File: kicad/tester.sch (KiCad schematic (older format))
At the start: 44 parts

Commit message: Schematic capture almost complete
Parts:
- added DS?: LCD16X2, WC1602A, symbol LCD16X2
- added R?: 270, symbol R_Small
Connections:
- net GND: now also DS?.16 (LED-)
- net VCC: now also R?.1
- net at IC?.11 ((PCINT21/OC0B/T1)PD5): now also DS?.6 (E)
- net at IC?.2 ((PCINT16/RXD)PD0): now also DS?.11 (D4)
- net at IC?.3 ((PCINT17/TXD)PD1): now also DS?.12 (D5)
- net at IC?.4 ((PCINT18/INT0)PD2): now also DS?.13 (D6)
- net at IC?.5 ((PCINT19/OC2B/INT1)PD3): now also DS?.14 (D7)
- net at IC?.6 ((PCINT20/XCK/T0)PD4): now also DS?.4 (RS)
- new net: DS?.15 (LED+), R?.2
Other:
- moved on the sheet: BT?, C?, CON?, D?, IC?, P?, Q?, R?, SW?, U?, Y?

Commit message: Schematic complete. Some refs des. incomplete
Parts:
- added R?: 10K, symbol R_Small
- added RV?: POT, symbol POT
- gave numbers to parts that had none: 19
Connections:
- net GND: now also C1.1, C3.1, DS?.1 (VSS), DS?.5 (R/W), RV?.3; no longer C1.2, C3.2
- net VCC: now also C3.2, DS?.2 (VDD), R?.1; no longer C3.1
- net at U1.21 (AREF): now also C1.2; no longer C1.1
- net at DS?.3 (VO): now also RV?.2
- new net: R?.2, RV?.1
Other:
- moved on the sheet: C1, C10, C3, C4, DS?

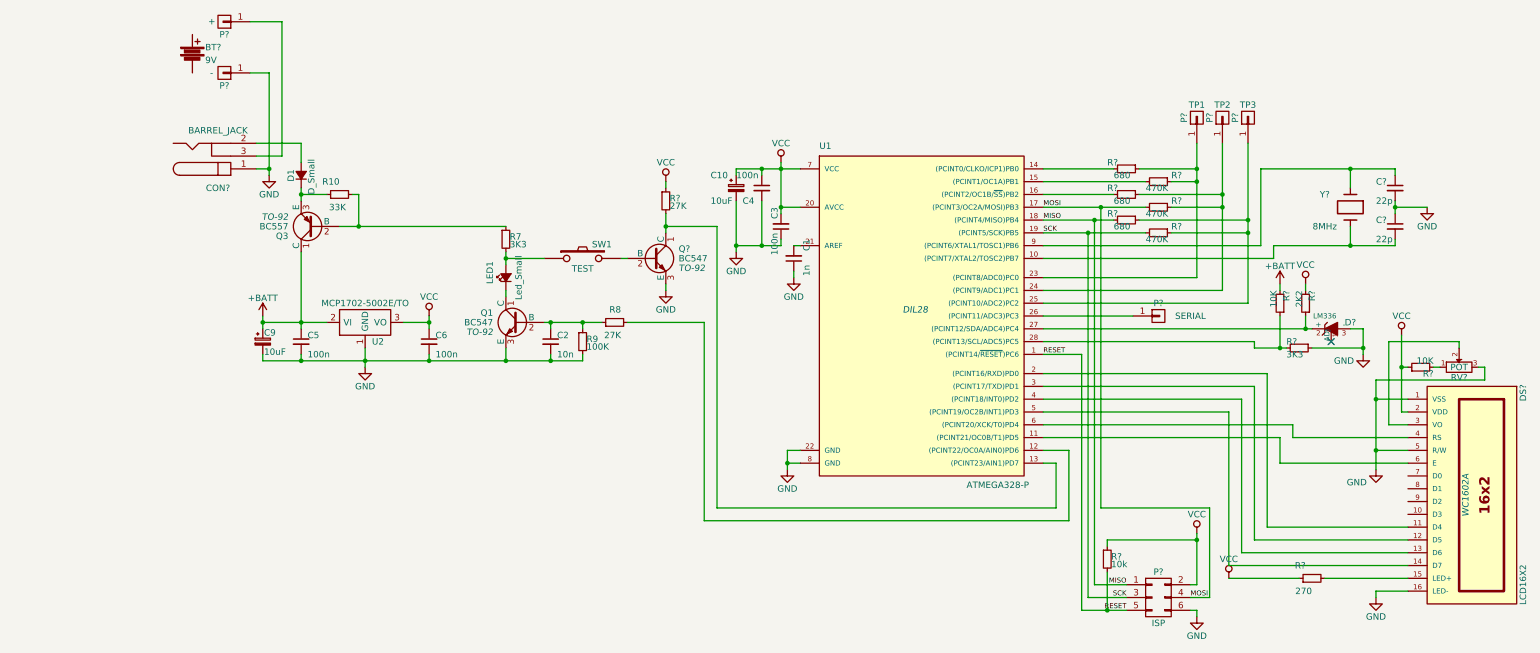
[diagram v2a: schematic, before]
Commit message: Board routing almost done
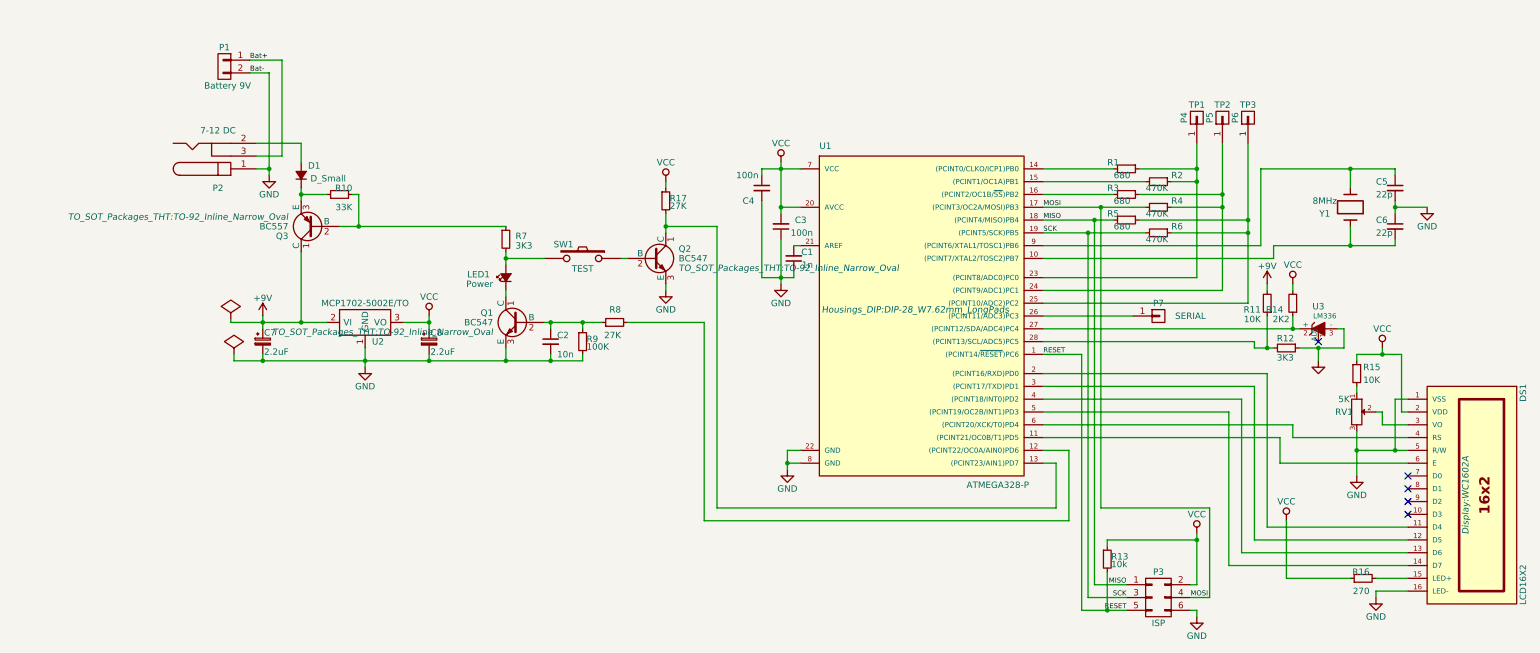
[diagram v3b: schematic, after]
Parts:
- removed BT?: 9V, symbol Battery
- removed C10: 10uF, symbol CP_Small
- removed C5, C6: 100n, symbol C_Small
- removed P?: +, symbol CONN_01X01
- removed P?: -, symbol CONN_01X01
- added C8: 2.2uF, Capacitors_ThroughHole:C_Radial_D6.3_L11.2_P2.5, symbol CP_Small
- added P1: Battery 9V, Connect:PINHEAD1-2, symbol CONN_01X02
- C1, C2: footprint (none) -> Capacitors_ThroughHole:C_Disc_D3_P2.5
- C3, C4: footprint (none) -> Capacitors_ThroughHole:C_Disc_D6_P5
- C5, C6: renamed from C?; footprint (none) -> Capacitors_ThroughHole:C_Disc_D3_P2.5
- C7: renamed from C9; value 10uF -> 2.2uF; footprint (none) -> Capacitors_ThroughHole:C_Radial_D6.3_L11.2_P2.5
- D1: footprint (none) -> Diodes_ThroughHole:Diode_DO-35_SOD27_Horizontal_RM10
- DS1: renamed from DS?; footprint WC1602A -> Display:WC1602A
- LED1: value Led_Small -> Power; footprint (none) -> LEDs:LED-3MM
- P2: renamed from CON?; value BARREL_JACK -> 7-12 DC; footprint (none) -> Connect:BARREL_JACK
- P3: renamed from P?; footprint (none) -> Pin_Headers:Pin_Header_Straight_2x03
- P4, P5, P6, P7: renamed from P?; footprint (none) -> Wire_Pads:SolderWirePad_single_1mmDrill
- Q1, Q3: footprint TO-92 -> TO_SOT_Packages_THT:TO-92_Inline_Narrow_Oval
- Q2: renamed from Q?; footprint TO-92 -> TO_SOT_Packages_THT:TO-92_Inline_Narrow_Oval
- R1, R11, R12, R13, R14, R15, R16, R17, R2, R3, R4, R5, R6: renamed from R?; footprint (none) -> Resistors_ThroughHole:Resistor_Horizontal_RM10mm
- R10, R7, R8, R9: footprint (none) -> Resistors_ThroughHole:Resistor_Horizontal_RM10mm
- RV1: renamed from RV?; value POT -> 5K; footprint (none) -> Potentiometers:Potentiometer_VishaySpectrol-Econtrim-Type36k
- SW1: footprint (none) -> Connect:PINHEAD1-2
- U1: footprint DIL28 -> Housings_DIP:DIP-28_W7.62mm_LongPads
- U2: footprint (none) -> TO_SOT_Packages_THT:TO-92_Inline_Narrow_Oval
- U3: renamed from D?; footprint (none) -> TO_SOT_Packages_THT:TO-92_Inline_Narrow_Oval
- Y1: renamed from Y?; footprint (none) -> Crystals:Crystal_HC49-U_Horizontal_Typ1
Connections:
- net GND: now also C8.2, P1.2 (P2)
- net VCC: now also C8.1
- net at C6.2, U1.10 ((PCINT7/XTAL2/TOSC2)PB7): now also Y1.1; no longer Y1.2
- net at C5.1, U1.9 ((PCINT6/XTAL1/TOSC1)PB6): now also Y1.2; no longer Y1.1
- net Bat+: now reaches P2.3
- net Bat+: now also P1.1 (P1)
- net at LED1.2 (A), R7.2: now also SW1.2; no longer SW1.1
- net at Q2.2 (B): now also SW1.1; no longer SW1.2
- net +BATT renamed +9V
- no-connect marks 1 -> 5
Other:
- moved on the sheet: R11, R12, R14, R15, R16, RV1, U3
